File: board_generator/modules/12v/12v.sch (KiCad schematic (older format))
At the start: 5 parts, among them J1 Screw_Terminal_01x01, J2 Screw_Terminal_01x01, X1 interface, X2 interface

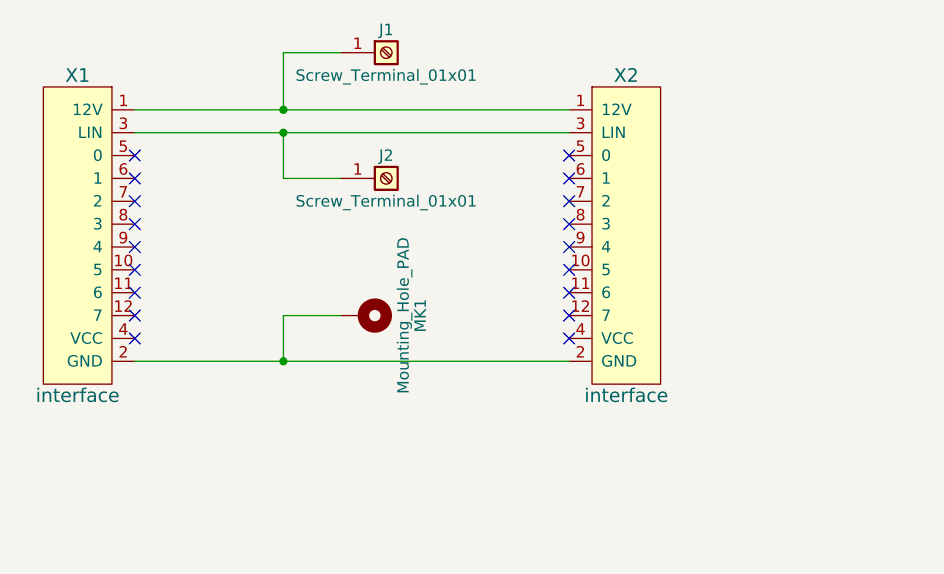
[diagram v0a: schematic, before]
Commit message: Using solder pads for 12v module
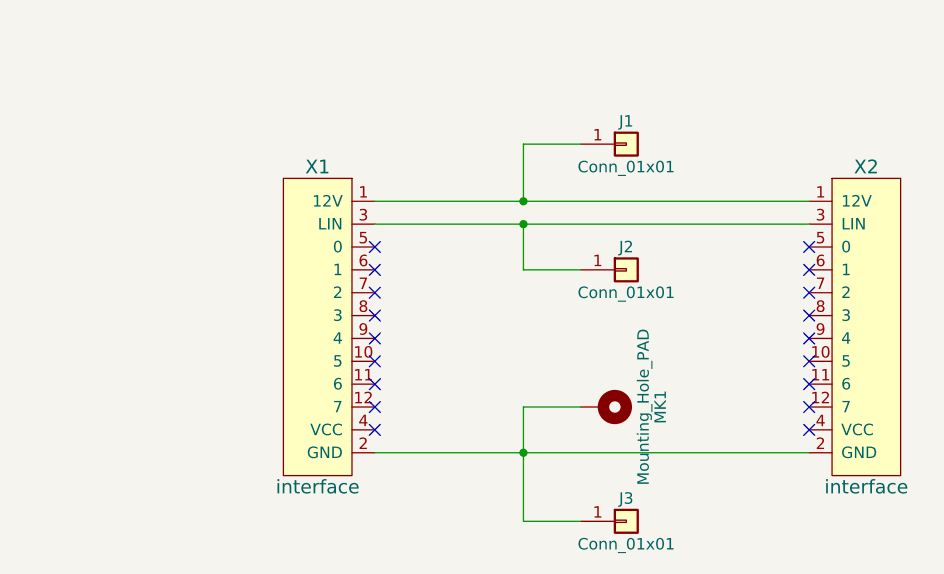
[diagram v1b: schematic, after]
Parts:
- removed J1, J2: Screw_Terminal_01x01, connectors:TERM_SCREW_M3, symbol Screw_Terminal_01x01
- added J1, J2, J3: Conn_01x01, Wire_Pads:SolderWirePad_single_SMD_5x10mm, symbol Conn_01x01
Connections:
- net at X1.1 (12V), X2.1 (12V): now also J1.1 (Pin_1)
- net at MK1.1, X1.2 (GND), X2.2 (GND): now also J3.1 (Pin_1)
- net at X1.3 (LIN), X2.3 (LIN): now also J2.1 (Pin_1)
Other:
- moved on the sheet: MK1, X1, X2
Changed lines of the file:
@@
 L interface X1
 U 1 1 59F014B9
-P 3900 3450
-F 0 "X1" H 3900 4150 60  0000 C CNN
-F 1 "interface" H 3900 2750 60  0000 C CNN
-F 2 "interface:interface" H 4150 4150 60  0001 C CNN
-F 3 "" H 4150 4150 60  0001 C CNN
-	1    3900 3450
+P 4950 3850
+F 0 "X1" H 4950 4550 60  0000 C CNN
+F 1 "interface" H 4950 3150 60  0000 C CNN
+F 2 "interface:interface" H 5200 4550 60  0001 C CNN
+F 3 "" H 5200 4550 60  0001 C CNN
+	1    4950 3850
 	1    0    0    -1
 $EndComp
-NoConn ~ 4150 3100
-NoConn ~ 4150 3200
-NoConn ~ 4150 3300
-NoConn ~ 4150 3400
-NoConn ~ 4150 3500
-NoConn ~ 4150 3600
-NoConn ~ 4150 3700
-NoConn ~ 4150 3800
-NoConn ~ 4150 3900
+NoConn ~ 5200 3500
+NoConn ~ 5200 3600
+NoConn ~ 5200 3700
+NoConn ~ 5200 3800
+NoConn ~ 5200 3900
+NoConn ~ 5200 4000
+NoConn ~ 5200 4100
+NoConn ~ 5200 4200
+NoConn ~ 5200 4300
 $Comp
-L Screw_Terminal_01x01 J1
-U 1 1 59F01553
-P 5250 2650
-F 0 "J1" H 5250 2750 50  0000 C CNN
-F 1 "Screw_Terminal_01x01" H 5250 2550 50  0000 C CNN
-F 2 "connectors:TERM_SCREW_M3" H 5250 2650 50  0001 C CNN
-F 3 "" H 5250 2650 50  0001 C CNN
-	1    5250 2650
+L interface X2
+U 1 1 59F01607
+P 7350 3850
+F 0 "X2" H 7350 4550 60  0000 C CNN
+F 1 "interface" H 7350 3150 60  0000 C CNN
+F 2 "interface:interface" H 7600 4550 60  0001 C CNN
+F 3 "" H 7600 4550 60  0001 C CNN
+	1    7350 3850
+	-1   0    0    -1
+$EndComp
+Wire Wire Line
+	5200 3300 7100 3300
+Wire Wire Line
+	5200 3400 7100 3400
+Wire Wire Line
+	5200 4400 7100 4400
+Wire Wire Line
+	6100 3050 5850 3050
+Wire Wire Line
+	5850 3050 5850 3300
+Connection ~ 5850 3300
+Wire Wire Line
+	5850 3600 5850 3400
+Connection ~ 5850 3400
+Wire Wire Line
+	6100 3600 5850 3600
+Wire Wire Line
+	6100 4200 5850 4200
+Wire Wire Line
+	5850 4200 5850 4700
+Connection ~ 5850 4400
+NoConn ~ 7100 3500
+NoConn ~ 7100 3600
+NoConn ~ 7100 3700
+NoConn ~ 7100 3800
+NoConn ~ 7100 3900
+NoConn ~ 7100 4000
+NoConn ~ 7100 4100
+NoConn ~ 7100 4200
+NoConn ~ 7100 4300
+$Comp
+L Mounting_Hole_PAD MK1
+U 1 1 59F01C27
+P 6200 4200
+F 0 "MK1" H 6200 4450 50  0000 C CNN
+F 1 "Mounting_Hole_PAD" H 6200 4375 50  0000 C CNN
+F 2 "Mounting_Holes:MountingHole_3.2mm_M3_Pad" H 6200 4200 50  0001 C CNN
+F 3 "" H 6200 4200 50  0001 C CNN
+	1    6200 4200
+	0    1    1    0
+$EndComp
+$Comp
+L Conn_01x01 J1
+U 1 1 5BDFD591
+P 6300 3050
+F 0 "J1" H 6300 3150 50  0000 C CNN
+F 1 "Conn_01x01" H 6300 2950 50  0000 C CNN
+F 2 "Wire_Pads:SolderWirePad_single_SMD_5x10mm" H 6300 3050 50  0001 C CNN
+F 3 "" H 6300 3050 50  0001 C CNN
+	1    6300 3050
 	1    0    0    -1
 $EndComp
 $Comp
-L Screw_Terminal_01x01 J2
-U 1 1 59F01590
-P 5250 3200
-F 0 "J2" H 5250 3300 50  0000 C CNN
-F 1 "Screw_Terminal_01x01" H 5250 3100 50  0000 C CNN
-F 2 "connectors:TERM_SCREW_M3" H 5250 3200 50  0001 C CNN
-F 3 "" H 5250 3200 50  0001 C CNN
-	1    5250 3200
+L Conn_01x01 J2
+U 1 1 5BDFD64E
+P 6300 3600
+F 0 "J2" H 6300 3700 50  0000 C CNN
+F 1 "Conn_01x01" H 6300 3500 50  0000 C CNN
+F 2 "Wire_Pads:SolderWirePad_single_SMD_5x10mm" H 6300 3600 50  0001 C CNN
+F 3 "" H 6300 3600 50  0001 C CNN
+	1    6300 3600
 	1    0    0    -1
 $EndComp
 $Comp
-L interface X2
-U 1 1 59F01607
-P 6300 3450
-F 0 "X2" H 6300 4150 60  0000 C CNN
-F 1 "interface" H 6300 2750 60  0000 C CNN
-F 2 "interface:interface" H 6550 4150 60  0001 C CNN
-F 3 "" H 6550 4150 60  0001 C CNN
-	1    6300 3450
-	-1   0    0    -1
+L Conn_01x01 J3
+U 1 1 5BDFD6FF
+P 6300 4700
+F 0 "J3" H 6300 4800 50  0000 C CNN
+F 1 "Conn_01x01" H 6300 4600 50  0000 C CNN
+F 2 "Wire_Pads:SolderWirePad_single_SMD_5x10mm" H 6300 4700 50  0001 C CNN
+F 3 "" H 6300 4700 50  0001 C CNN
+	1    6300 4700
+	1    0    0    -1
 $EndComp
 Wire Wire Line
-	4150 2900 6050 2900
-Wire Wire Line
-	4150 3000 6050 3000
-Wire Wire Line
-	4150 4000 6050 4000
-Wire Wire Line
-	5050 2650 4800 2650
-Wire Wire Line
-	4800 2650 4800 2900
-Connection ~ 4800 2900
-Wire Wire Line
-	4800 3200 4800 3000
-Connection ~ 4800 3000
-Wire Wire Line
-	5050 3200 4800 3200
-Wire Wire Line
-	5050 3800 4800 3800
-Wire Wire Line
-	4800 3800 4800 4000
-Connection ~ 4800 4000
-NoConn ~ 6050 3100
-NoConn ~ 6050 3200
-NoConn ~ 6050 3300
-NoConn ~ 6050 3400
-NoConn ~ 6050 3500
-NoConn ~ 6050 3600
-NoConn ~ 6050 3700
-NoConn ~ 6050 3800
-NoConn ~ 6050 3900
-$Comp
-L Mounting_Hole_PAD MK1
-U 1 1 59F01C27
-P 5150 3800
-F 0 "MK1" H 5150 4050 50  0000 C CNN
-F 1 "Mounting_Hole_PAD" H 5150 3975 50  0000 C CNN
-F 2 "Mounting_Holes:MountingHole_3.2mm_M3_Pad" H 5150 3800 50  0001 C CNN
-F 3 "" H 5150 3800 50  0001 C CNN
-	1    5150 3800
-	0    1    1    0
-$EndComp
+	5850 4700 6100 4700
 $EndSCHEMATC
